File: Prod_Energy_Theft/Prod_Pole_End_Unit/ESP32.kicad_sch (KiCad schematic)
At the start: 24 parts, among them J14 U.FL-R-SMT_01_, U13 USBLC6-2SC6, U14 E32-433T20S, U15 CP2102N-Axx-xQFN20, U16 ESP32-C6-MINI-1

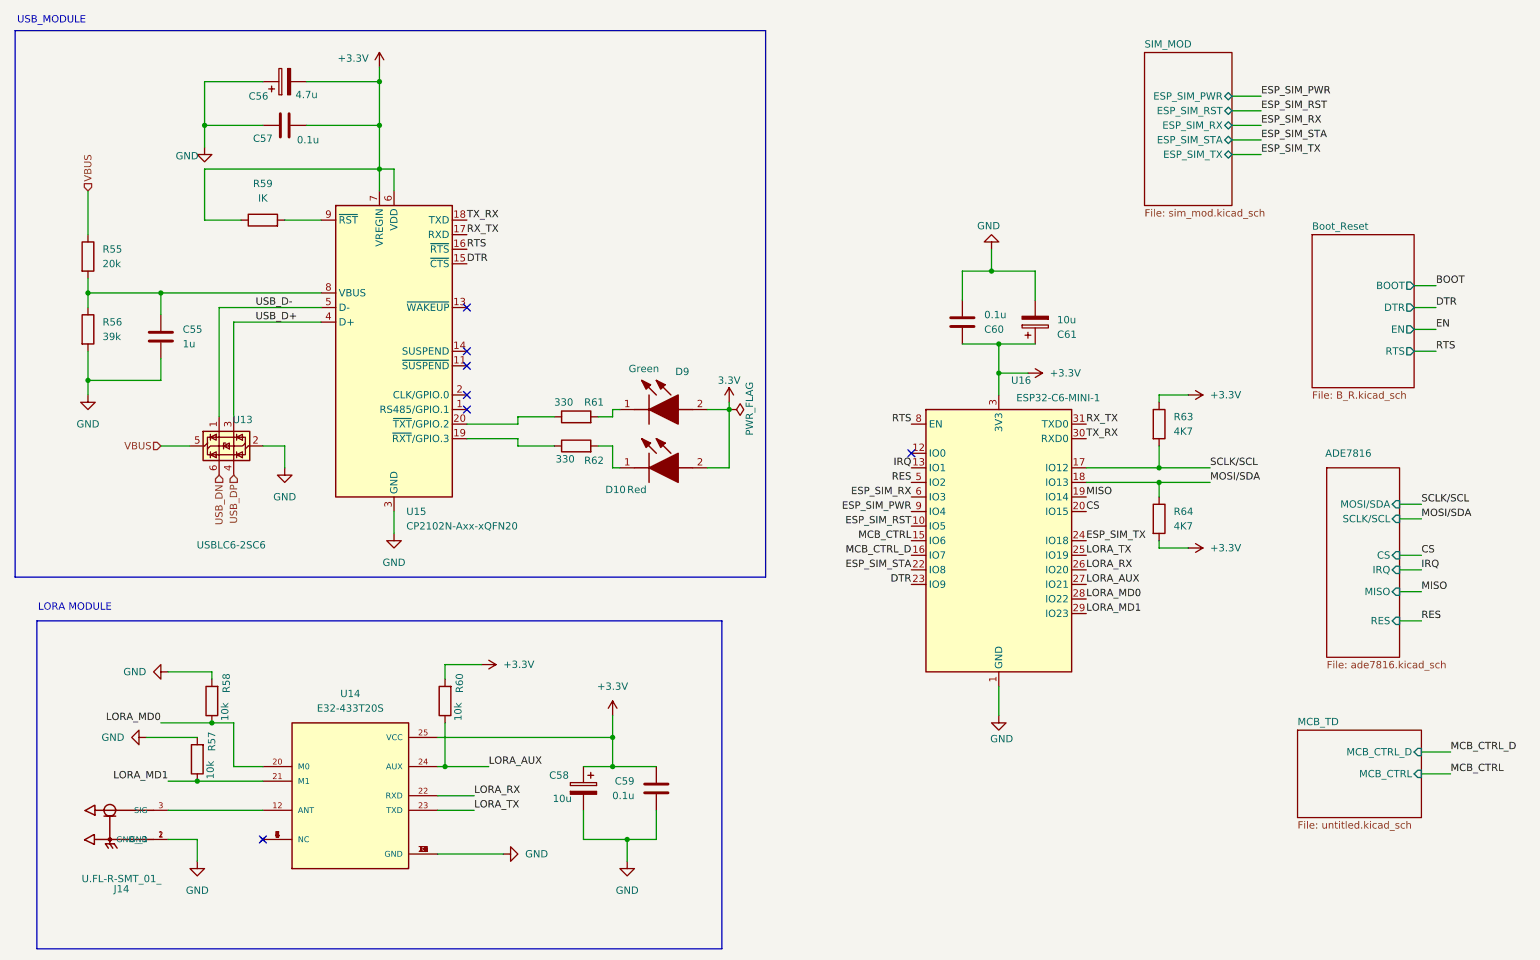
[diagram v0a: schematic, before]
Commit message: Chnages in power and ADE7816
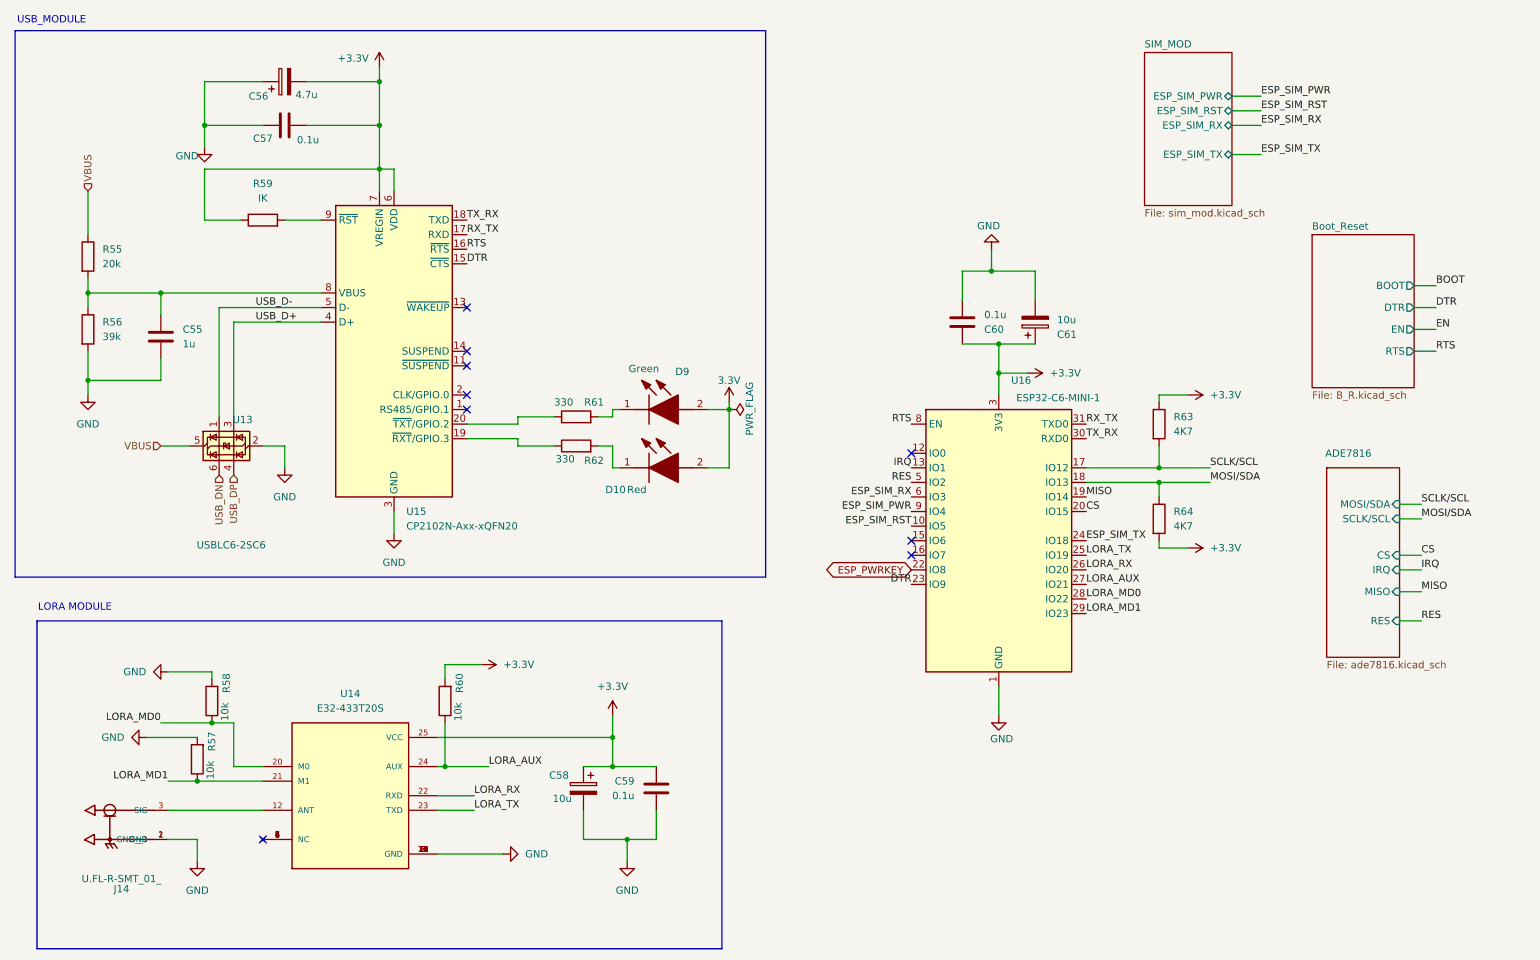
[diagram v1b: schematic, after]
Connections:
- net ESP_SIM_STA renamed ESP_PWRKEY
- net MCB_CTRL: no longer names the net of U16.15 (IO6)
- net MCB_CTRL_D: no longer names the net of U16.16 (IO7)
- no-connect marks 7 -> 9
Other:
- removed sheet MCB_TD
- sheet SIM_MOD ports: added none; removed ESP_SIM_STA
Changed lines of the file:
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@@
 	)
 	(no_connect
+		(at 173.99 109.22)
+	)
+	(no_connect
 		(at 96.52 83.82)
 	)
@@
 	)
 	(no_connect
+		(at 173.99 106.68)
+	)
+	(no_connect
 		(at 96.52 73.66)
 	)
@@
 	(wire
 		(pts
-			(xy 229.87 36.83) (xy 234.95 36.83)
-		)
-		(stroke
-			(width 0)
-			(type default)
-		)
-	)
-	(wire
-		(pts
 			(xy 189.23 81.28) (xy 189.23 77.47)
 		)
@@
 	(wire
 		(pts
-			(xy 267.97 147.32) (xy 262.89 147.32)
-		)
-		(stroke
-			(width 0)
-			(type default)
-		)
-	)
-	(wire
-		(pts
 			(xy 92.71 138.43) (xy 92.71 146.05)
 		)
@@
 	(wire
 		(pts
-			(xy 262.89 143.51) (xy 267.97 143.51)
-		)
-		(stroke
-			(width 0)
-			(type default)
-		)
-	)
-	(wire
-		(pts
 			(xy 30.48 60.96) (xy 30.48 63.5)
 		)
@@
 		)
 	)
-	(label "MCB_CTRL"
-		(at 173.99 106.68 180)
-		(effects
-			(font
-				(size 1.27 1.27)
-			)
-			(justify right bottom)
-		)
-	)
 	(label "ESP_SIM_TX"
 		(at 234.95 39.37 0)
@@
 		)
 	)
-	(label "ESP_SIM_STA"
-		(at 234.95 36.83 0)
-		(effects
-			(font
-				(size 1.27 1.27)
-			)
-			(justify left bottom)
-		)
-	)
 	(label "RES"
 		(at 173.99 96.52 180)
@@
 		)
 	)
-	(label "ESP_SIM_STA"
-		(at 173.99 111.76 180)
-		(effects
-			(font
-				(size 1.27 1.27)
-			)
-			(justify right bottom)
-		)
-	)
 	(label "MOSI{slash}SDA"
 		(at 262.89 102.87 0)
@@
 		)
 	)
-	(label "MCB_CTRL_D"
-		(at 267.97 143.51 0)
-		(effects
-			(font
-				(size 1.27 1.27)
-			)
-			(justify left bottom)
-		)
-	)
-	(label "MCB_CTRL_D"
-		(at 173.99 109.22 180)
-		(effects
-			(font
-				(size 1.27 1.27)
-			)
-			(justify right bottom)
-		)
-	)
 	(label "LORA_RX"
 		(at 204.47 111.76 0)
@@
 		)
 	)
-	(label "MCB_CTRL"
-		(at 267.97 147.32 0)
+	(global_label "ESP_PWRKEY"
+		(shape bidirectional)
+		(at 173.99 111.76 180)
 		(effects
 			(font
 				(size 1.27 1.27)
 			)
-			(justify left bottom)
+			(justify right)
+		)
+		(property "Intersheetrefs" "${INTERSHEET_REFS}"
+			(at 173.99 111.76 0)
+			(effects
+				(font
+					(size 1.27 1.27)
+				)
+				(hide yes)
+			)
 		)
 	)
@@
 			)
 		)
-		(pin "ESP_SIM_STA" bidirectional
-			(at 229.87 36.83 0)
-			(effects
-				(font
-					(size 1.27 1.27)
-				)
-				(justify right)
-			)
-		)
 		(pin "ESP_SIM_TX" bidirectional
 			(at 229.87 39.37 0)
@@
 				)
 			)
-		)
-	)
-	(sheet
-		(at 241.3 139.7)
-		(size 21.59 15.24)
-		(exclude_from_sim no)
-		(in_bom yes)
-		(on_board yes)
-		(dnp no)
-		(fields_autoplaced yes)
-		(stroke
-			(width 0.1524)
-			(type solid)
-		)
-		(fill
-			(color 0 0 0 0.0000)
-		)
-		(property "Sheetname" "MCB_TD"
-			(at 241.3 138.9884 0)
-			(effects
-				(font
-					(size 1.27 1.27)
-				)
-				(justify left bottom)
-			)
-		)
-		(property "Sheetfile" "untitled.kicad_sch"
-			(at 241.3 155.5246 0)
-			(effects
-				(font
-					(size 1.27 1.27)
-				)
-				(justify left top)
-			)
-		)
-		(pin "MCB_CTRL" input
-			(at 262.89 147.32 0)
-			(effects
-				(font
-					(size 1.27 1.27)
-				)
-				(justify right)
-			)
-		)
-		(pin "MCB_CTRL_D" input
-			(at 262.89 143.51 0)
-			(effects
-				(font
-					(size 1.27 1.27)
-				)
-				(justify right)
-			)
-		)
-		(instances
-			(project "Prod_Pole_End_Unit"
-				(path "/6f618807-d67d-4ead-90e4-cf8a7a59b747/5ab1b14f-4aa4-492d-8e7b-cd8ac008f654"
-					(page "9")
-				)
-			)

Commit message: PCB
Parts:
- C56, C58: footprint Footprints.kicad_mod:T491A -> Capacitor_SMD:C_0805_2012Metric
- D10, D9: footprint Footprints:LEDC2012X120N -> theftdetection:LEDC2012X120N
- J14: footprint U.FL-R-SMT_01_:HRS_U.FL-R-SMT_01_ -> theftdetection:HRS_U.FL-R-SMT_01_
- U14: footprint E32-433T20S:MODULE_E32-433T20S -> theftdetection:MODULE_E32-433T20S
- U15: footprint Package_DFN_QFN:SiliconLabs_QFN-20-1EP_3x3mm_P0.5mm -> theftdetection:IC_CP2102N-A01-GQFN20
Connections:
- net 3.3V is gone; now on net +3.3V: D10.2 (A), D9.2 (A)
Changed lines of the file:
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@@
 			)
 		)
-		(property "Footprint" "Footprints.kicad_mod:T491A"
+		(property "Footprint" "Capacitor_SMD:C_0805_2012Metric"
 			(at 115.8748 153.67 0)
 			(effects
@@
 			)
 		)
-		(property "Footprint" "U.FL-R-SMT_01_:HRS_U.FL-R-SMT_01_"
+		(property "Footprint" "theftdetection:HRS_U.FL-R-SMT_01_"
 			(at 34.29 156.21 0)
 			(effects
@@
 			)
 		)
-		(property "Footprint" "E32-433T20S:MODULE_E32-433T20S"
+		(property "Footprint" "theftdetection:MODULE_E32-433T20S"
 			(at 76.2 151.13 0)
 			(effects
@@
 			)
 		)
-		(property "Footprint" "Footprints:LEDC2012X120N"
+		(property "Footprint" "theftdetection:LEDC2012X120N"
 			(at 135.89 177.47 0)
 			(effects
@@
 			)
 		)
-		(property "Value" "3.3V"
+		(property "Value" "+3.3V"
 			(at 142.24 78.74 0)
 			(do_not_autoplace yes)
@@
 				(path "/6f618807-d67d-4ead-90e4-cf8a7a59b747/5ab1b14f-4aa4-492d-8e7b-cd8ac008f654"
 					(reference "#PWR0119")
-					(unit 1)
-				)
-			)
-		)
-	)
-	(symbol
-		(lib_id "power:PWR_FLAG")
-		(at 142.24 83.82 270)
-		(unit 1)
-		(exclude_from_sim no)
-		(in_bom yes)
-		(on_board yes)
-		(dnp no)
-		(property "Reference" "#FLG06"
-			(at 144.145 83.82 0)
-			(effects
-				(font
-					(size 1.27 1.27)
-				)
-				(hide yes)
-			)
-		)
-		(property "Value" "PWR_FLAG"
-			(at 145.796 78.994 0)
-			(effects
-				(font
-					(size 1.27 1.27)
-				)
-				(justify left)
-			)
-		)
-		(property "Footprint" ""
-			(at 142.24 83.82 0)
-			(effects
-				(font
-					(size 1.27 1.27)
-				)
-				(hide yes)
-			)
-		)
-		(property "Datasheet" "~"
-			(at 142.24 83.82 0)
-			(effects
-				(font
-					(size 1.27 1.27)
-				)
-				(hide yes)
-			)
-		)
-		(property "Description" "Special symbol for telling ERC where power comes from"
-			(at 142.24 83.82 0)
-			(effects
-				(font
-					(size 1.27 1.27)
-				)
-				(hide yes)
-			)
-		)
-		(pin "1"
-		)
-		(instances
-			(project "Prod_Pole_End_Unit"
-				(path "/6f618807-d67d-4ead-90e4-cf8a7a59b747/5ab1b14f-4aa4-492d-8e7b-cd8ac008f654"
-					(reference "#FLG06")
 					(unit 1)
 				)
@@
 			)
 		)
-		(property "Footprint" "Footprints.kicad_mod:T491A"
+		(property "Footprint" "Capacitor_SMD:C_0805_2012Metric"
 			(at 68.58 25.7048 0)
 			(effects
@@
 			)
 		)
-		(property "Footprint" "Package_DFN_QFN:SiliconLabs_QFN-20-1EP_3x3mm_P0.5mm"
+		(property "Footprint" "theftdetection:IC_CP2102N-A01-GQFN20"
 			(at 115.57 100.33 0)
 			(effects
@@
 			)
 		)
-		(property "Footprint" "Footprints:LEDC2012X120N"
+		(property "Footprint" "theftdetection:LEDC2012X120N"
 			(at 135.89 187.63 0)
 			(effects
